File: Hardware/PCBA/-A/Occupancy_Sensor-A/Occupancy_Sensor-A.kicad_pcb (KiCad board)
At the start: 4 copper layers, 30 x 30 mm, 75 parts, among them J1 USB_C_Receptacle, J2 Conn_02x05_Odd_Even, Q1 2N7002, Q2 2N7002, Q3 2N7002, Q4 2N7002, Q5 2N7002, SW1 SW_SPDT, SW2 SW_Push, U1 TPS7A0333PDBVR, U2 VL53L8CX, U3 ECMF02-2AMX6, U4 TPS7A03185PDQNR, U5 TCS3430, U6 STM32WB55CGUx, Y2 NX2016SA_32M, Y3 NX2012_32K768

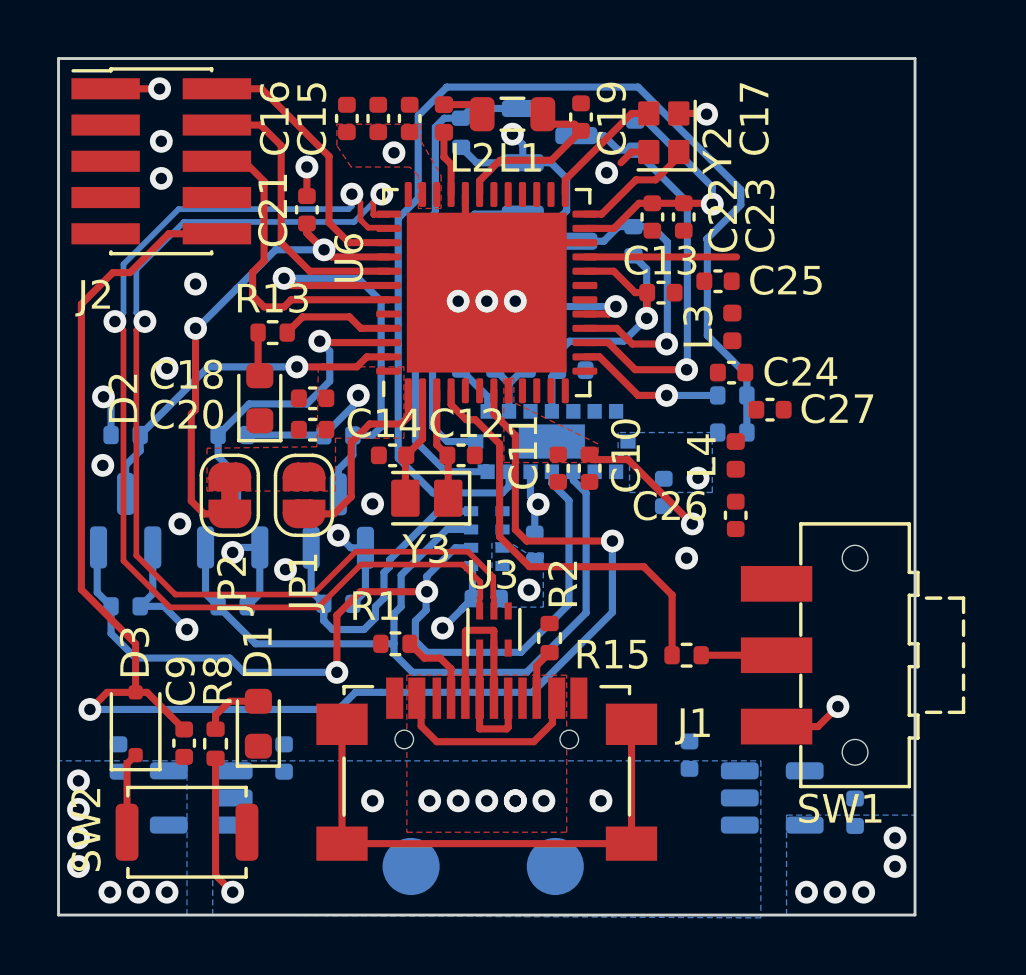
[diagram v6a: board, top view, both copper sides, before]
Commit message: Layout fixes, boot selector, testpoints
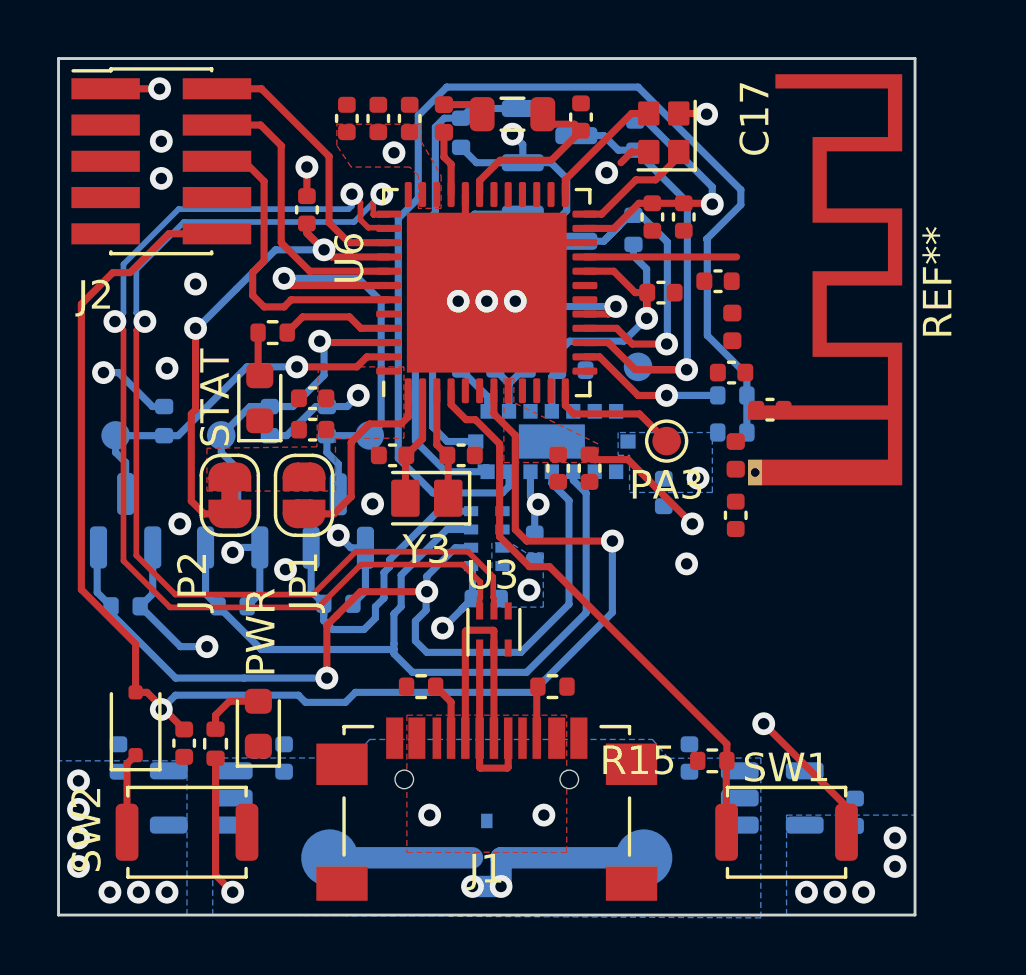
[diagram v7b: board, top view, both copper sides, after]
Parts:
- added Q6: DMG1012T, Package_TO_SOT_SMD:SOT-523, B.Cu at (145.0, 127.3)
- added REF**: Texas_SWRA117D_2.4GHz_Left, RF_Antenna:Texas_SWRA117D_2.4GHz_Left, F.Cu at (154.4, 112.4)
- added TP3: SCL, TestPoint:TestPoint_Pad_D1.0mm, B.Cu at (135.7, 113.2)
- added TP4: SDA, TestPoint:TestPoint_Pad_D1.0mm, B.Cu at (132.0, 113.2)
- added TP5: INTT, TestPoint:TestPoint_Pad_D1.0mm, B.Cu at (150.3, 110.8)
- added TP6: PA3, TestPoint:TestPoint_Pad_D1.0mm, F.Cu at (151.3, 113.4)
- added TP7: INTC, TestPoint:TestPoint_Pad_D1.0mm, B.Cu at (140.9, 113.2)
- D1: value LED -> PWR
- D2: value LED -> STAT
- SW1: value SW_SPDT -> SW_Push; footprint Button_Switch_SMD:SW_SPDT_CK-JS102011SAQN -> Button_Switch_SMD:SW_Push_SPST_NO_Alps_SKRK
- moved SW1 6.65 mm to (155.5, 127.1), turned to 0 degrees
- moved R15 3.81 mm to (152.9, 124.6)
- moved TP2 3.11 mm to (150.5, 128.0)
- moved TP1 2.87 mm to (139.5, 128.0)
- moved R1 1.75 mm to (142.7, 122.0)
- moved R2 1.70 mm to (147.3, 122.0), turned to 0 degrees
- moved R20 1.44 mm to (133.7, 112.7), turned to -90 degrees
- moved J1 1.40 mm to (145.0, 128.9)
- moved R18 1.39 mm to (137.4, 112.7), turned to 90 degrees
- moved R17 0.64 mm to (139.4, 112.7), turned to -90 degrees
- moved R10 0.40 mm to (150.1, 106.0)
- moved C6 0.10 mm to (152.1, 124.5)
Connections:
- R15 pad 1: Net-(SW1-B) -> BOOT
- R15 pad 2: BOOT -> GND
- SW1 pad 1: +3.3V -> BOOT
- SW1 pad 2: Net-(SW1-B) -> +3.3V
- TP1 pad 1: VBUS -> Net-(Q6-S)
- U6 pad 10: /PA1 -> unconnected-(U6-PA1-Pad10)
- U6 pad 11: /PA2 -> unconnected-(U6-PA2-Pad11)
- U6 pad 12: /PA3 -> Net-(U6-PA3)
- U6 pad 13: /PA4 -> unconnected-(U6-PA4-Pad13)
- U6 pad 18: /PA9 -> unconnected-(U6-PA9-Pad18)
- U6 pad 19: /PB2 -> unconnected-(U6-PB2-Pad19)
- U6 pad 28: /PB0 -> unconnected-(U6-PB0-Pad28)
- U6 pad 29: /PB1 -> unconnected-(U6-PB1-Pad29)
- U6 pad 36: /PA10 -> unconnected-(U6-PA10-Pad36)
- U6 pad 44: /PB4 -> unconnected-(U6-PB4-Pad44)
- U6 pad 5: /PB8 -> unconnected-(U6-PB8-Pad5)
- U6 pad 6: /PB9 -> unconnected-(U6-PB9-Pad6)
- U6 pad 9: /PA0 -> unconnected-(U6-PA0-Pad9)
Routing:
- net unconnected-(J1-SHIELD-PadS1): track 18.5 -> 0.00 mm
- net +1V8: track 86.7 -> 96.0 mm
- net VBUS: track 12.5 -> 4.94 mm, vias 7 -> 3
- net GND: track 11.6 -> 18.1 mm, vias 18 -> 17
- net BOOT: track 15.0 -> 20.1 mm
- net Net-(U6-PA3): track 0.00 -> 4.58 mm
- net Net-(Q6-S): track 0.00 -> 4.50 mm
- net NRST: track 55.2 -> 51.0 mm
- net +3.3V: track 35.6 -> 39.0 mm
- net Net-(U3-D-_in): track 5.72 -> 8.52 mm
- net Net-(SW1-B): track 2.64 -> 0.00 mm
- net INT_TOF_3V3: track 14.7 -> 16.4 mm
- net SYNC_3V3: track 10.3 -> 12.0 mm
- net Net-(U3-D+_in): track 4.88 -> 6.22 mm
- net INT_CLR_3V3: track 15.3 -> 16.1 mm
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
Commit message: RF layout
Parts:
- removed REF**: Texas_SWRA117D_2.4GHz_Left, RF_Antenna:Texas_SWRA117D_2.4GHz_Left
- added C28: ~, Capacitor_SMD:C_0402_1005Metric, F.Cu at (155.4, 116.1)
- added J3: Conn_Coaxial, Connector_Coaxial:U.FL_Molex_MCRF_73412-0110_Vertical, F.Cu at (157.3, 122.5)
- added U7: ~, Occupancy_Sensor_Custom_Footprints:LFB182G45CGFD436, F.Cu at (154.2, 112.1)
- L3: value 10n -> 2.7nH
- L4: value L -> 3.6nH
- moved R12 10.4 mm to (154.3, 102.7), turned to -90 degrees
- moved R11 9.12 mm to (153.0, 102.7), turned to 90 degrees
- moved C27 7.02 mm to (155.4, 119.3)
- moved C24 4.05 mm to (153.7, 107.0), turned to 0 degrees
- moved L4 3.98 mm to (154.9, 117.7), turned to -90 degrees
- moved C25 2.25 mm to (153.8, 110.0), turned to 0 degrees
- moved C26 1.91 mm to (154.9, 114.5), turned to -90 degrees
- moved L3 1.01 mm to (153.2, 108.5), turned to -90 degrees
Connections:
- C24 pad 1: Antenna -> RF
- C27 pad 1: Net-(AE1-A) -> Net-(J3-In)
- L3 pad 1: Net-(L1-Pad2) -> RF
- L3 pad 2: Net-(U4-VLXSMPS) -> Net-(C25-Pad1)
- L4 pad 1: unconnected-(L4-Pad1) -> Net-(C26-Pad2)
- L4 pad 2: unconnected-(L4-Pad2) -> Net-(J3-In)
- U6 pad 21: /RF1 -> RF
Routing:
- net +1V8: track 96.0 -> 76.3 mm
- net /LPn_1V8: track 40.1 -> 29.9 mm
- net LPn_3V3: track 5.21 -> 14.1 mm
- net RF: track 0.00 -> 5.60 mm
- net /RF1: track 5.31 -> 0.00 mm
- net Net-(J3-In): track 0.00 -> 4.40 mm
- net Net-(C25-Pad1): track 0.00 -> 2.91 mm
- net Net-(C26-Pad2): track 0.00 -> 2.25 mm
- net Net-(C26-Pad1): track 0.00 -> 1.60 mm
- net GND: track 18.1 -> 17.1 mm
